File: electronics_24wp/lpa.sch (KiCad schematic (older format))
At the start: 28 parts, among them IC1 ATMEGA328-A, P1 CONN_2, P2 CONN_3X2, U1 SD_CARD, U2 LD1117S33, X1 CRYSTAL_SMD

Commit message: Changed orientation of error LED.
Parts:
- ERR1: symbol LED -> LED-INV
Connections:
- net GND: now also ERR1.2 (K); no longer ERR1.1 (K)
- net at R_ERR1.2: now also ERR1.1 (A); no longer ERR1.2 (A)
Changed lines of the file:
@@
 $EndComp
 $Comp
-L LED ERR1
+L LED-INV ERR1
 U 1 1 5356E77E
 P 4750 6550
@@
 F 3 "~" H 4750 6550 60  0000 C CNN
 	1    4750 6550
-	-1   0    0    -1
+	1    0    0    1
 $EndComp
 $Comp

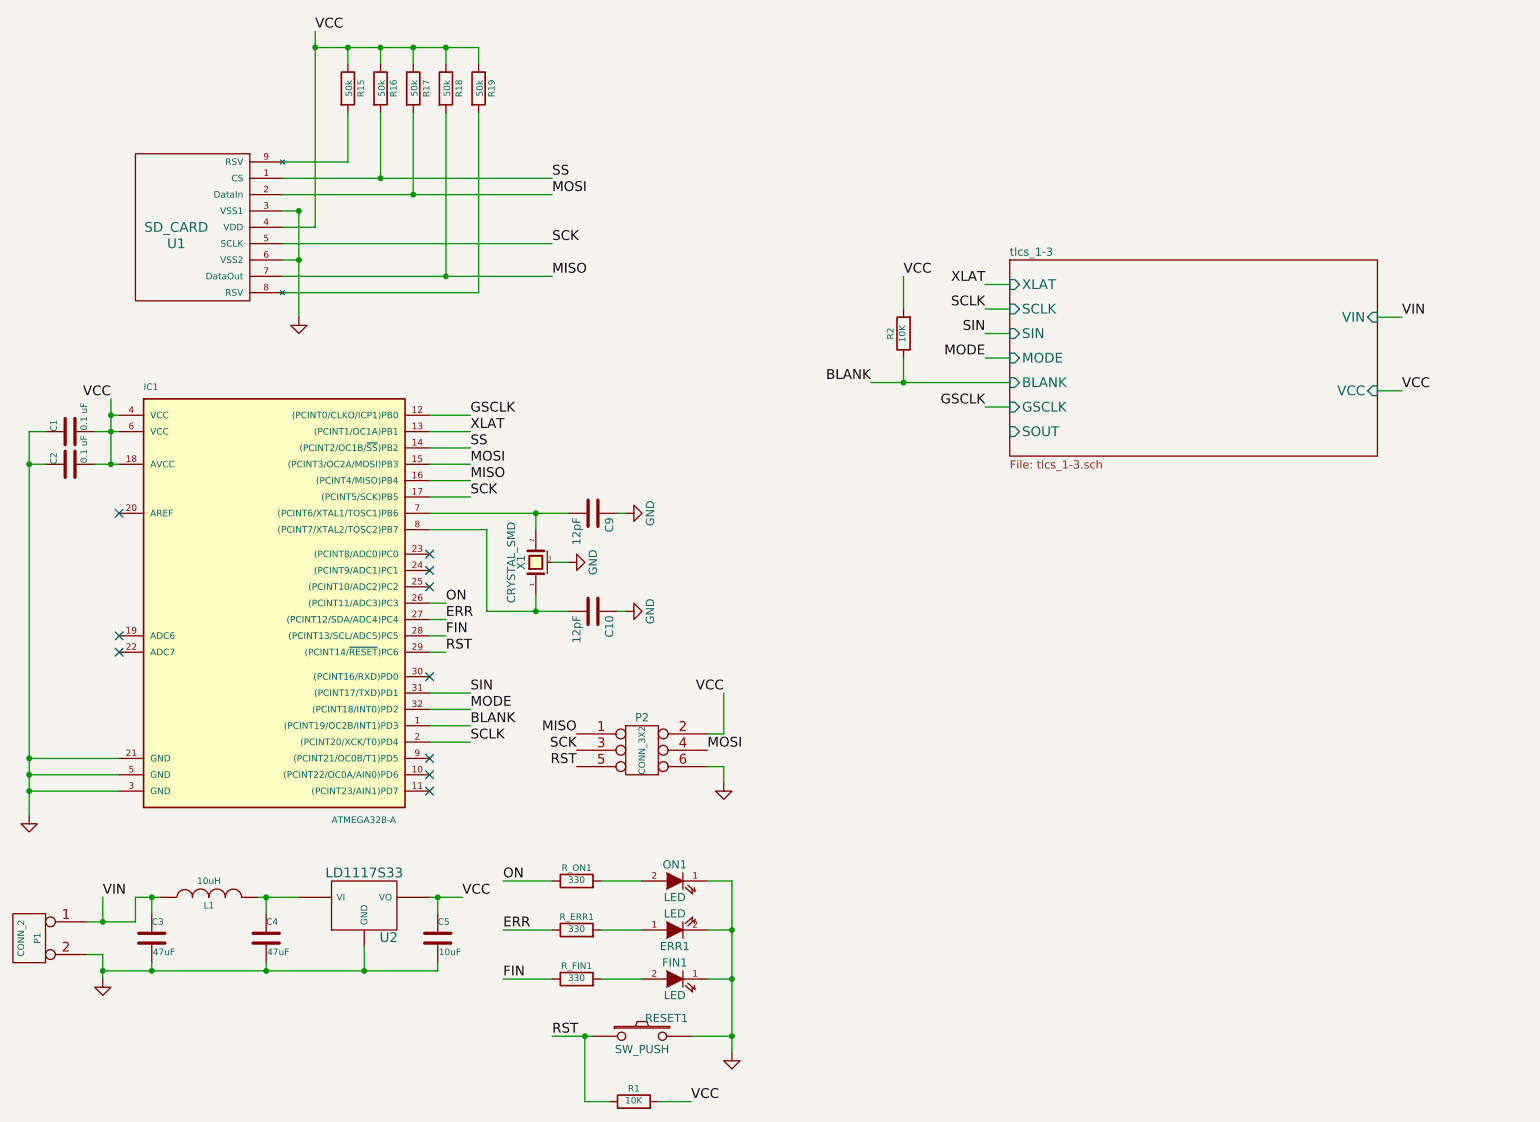
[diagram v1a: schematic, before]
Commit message: Removed pullup resistors from SD card socket.
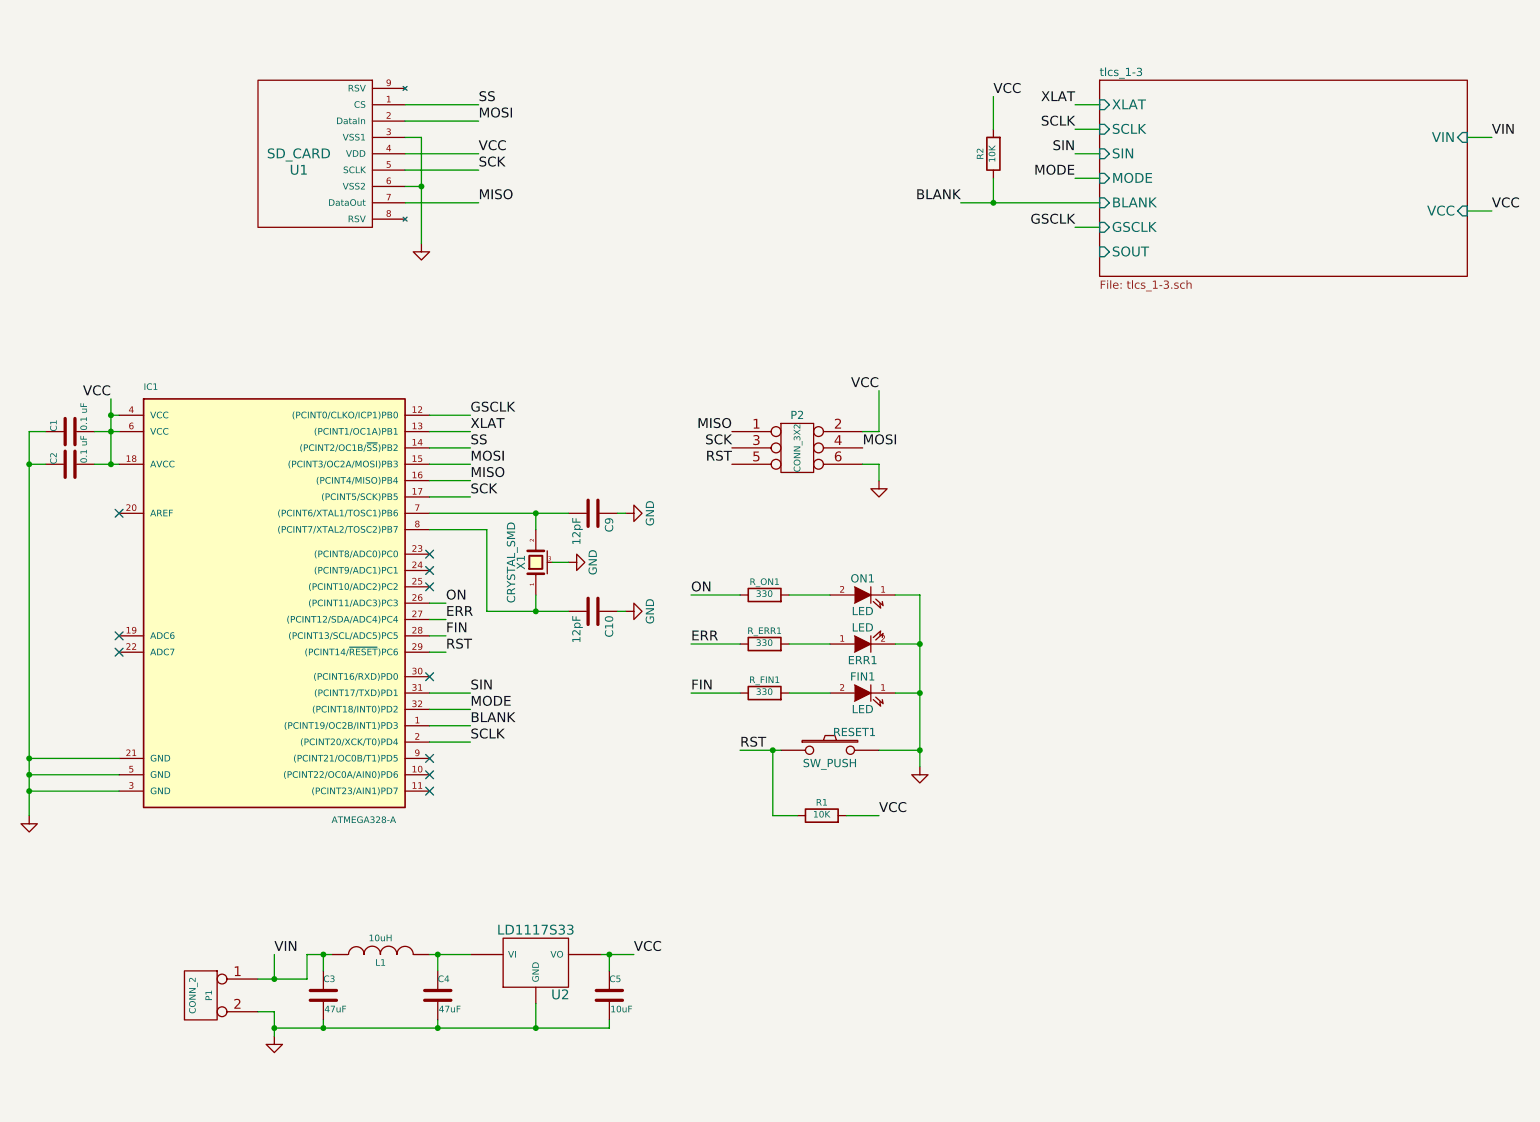
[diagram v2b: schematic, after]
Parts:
- removed R15, R16, R17, R18, R19: 50k, LPA_parts:SM0805, symbol R
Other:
- moved on the sheet: C3, C4, C5, ERR1, FIN1, L1, ON1, P1, P2, R1, R2, RESET1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

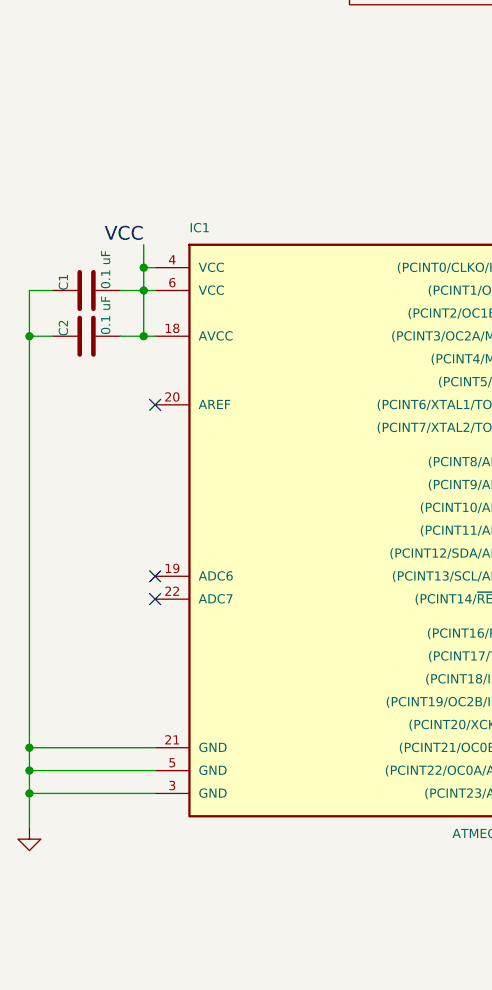
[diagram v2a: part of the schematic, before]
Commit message: Added one more decoupling resistor to uC.
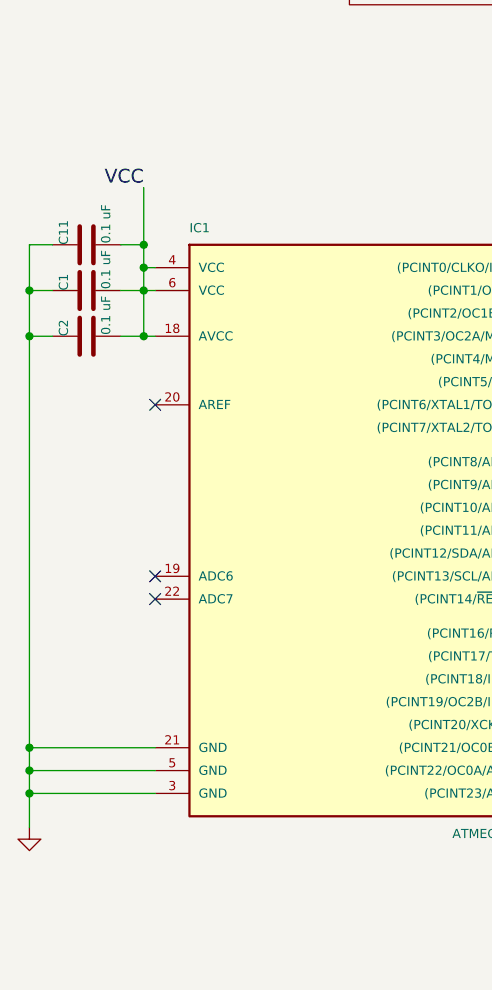
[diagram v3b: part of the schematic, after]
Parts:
- added C11: 0.1 uF, LPA_parts:SM0805, symbol C
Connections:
- net GND: now also C11.1
- net VCC: now also C11.2
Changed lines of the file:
@@
 Text Label 3500 3500 0    60   ~ 0
 XLAT
-Text Label 1300 3300 2    60   ~ 0
+Text Label 1300 3050 2    60   ~ 0
 VCC
 NoConn ~ 1350 4000
@@
 Wire Wire Line
 	3250 5100 3500 5100
-Wire Wire Line
-	800  3500 900  3500
 Connection ~ 800  3700
-Wire Wire Line
-	800  3700 900  3700
 Wire Wire Line
 	3600 4600 4100 4600
@@
 	1200 3700 1350 3700
 Wire Wire Line
-	1300 3300 1300 3700
+	1300 3050 1300 3700
 Wire Wire Line
 	1350 3400 1300 3400
@@
 	1200 3500 1350 3500
 Wire Wire Line
-	800  3500 800  5850
+	800  3300 800  5850
 Wire Wire Line
 	800  5500 1350 5500
@@
 Wire Wire Line
 	5450 4500 5700 4500
+Wire Wire Line
+	800  3500 900  3500
+Wire Wire Line
+	800  3700 900  3700
+$Comp
+L C C11
+U 1 1 569F3F37
+P 1050 3300
+F 0 "C11" H 1050 3400 40  0000 L CNN
+F 1 "0.1 uF" H 1056 3215 40  0000 L CNN
+F 2 "LPA_parts:SM0805" H 1088 3150 30  0001 C CNN
+F 3 "~" H 1050 3300 60  0000 C CNN
+	1    1050 3300
+	0    -1   -1   0
+$EndComp
+Wire Wire Line
+	800  3300 900  3300
+Connection ~ 800  3500
+Wire Wire Line
+	1200 3300 1300 3300
+Connection ~ 1300 3300
 $EndSCHEMATC

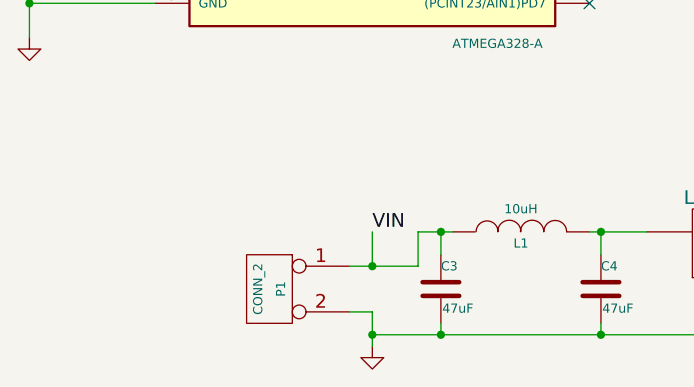
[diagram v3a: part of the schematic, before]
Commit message: Replaced power connector by barrel jack.
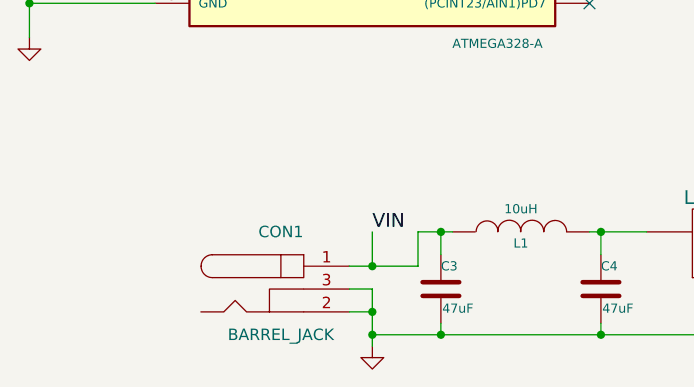
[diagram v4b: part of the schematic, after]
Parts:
- removed P1: CONN_2, LPA_parts:CONNECTOR_2X1_3960um, symbol CONN_2
- added CON1: BARREL_JACK, Connect:BARREL_JACK, symbol BARREL_JACK
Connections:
- net GND: now also CON1.2, CON1.3
- net VIN: now also CON1.1
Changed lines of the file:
@@
 VCC
-$Comp
-L CONN_2 P1
-U 1 1 5213FDDC
-P 1850 6950
-F 0 "P1" V 1800 6950 40  0000 C CNN
-F 1 "CONN_2" V 1900 6950 40  0000 C CNN
-F 2 "LPA_parts:CONNECTOR_2X1_3960um" H 1850 6950 60  0001 C CNN
-F 3 "" H 1850 6950 60  0000 C CNN
-	1    1850 6950
-	-1   0    0    -1
-$EndComp
 $Comp
 L CONN_3X2 P2
@@
 	2500 6850 2500 6700
 Wire Wire Line
-	2300 7050 2300 7200
+	2300 6950 2300 7200
 Wire Wire Line
 	2200 7050 2300 7050
@@
 	1200 3300 1300 3300
 Connection ~ 1300 3300
+$Comp
+L BARREL_JACK CON1
+U 1 1 56A00A09
+P 1900 6950
+F 0 "CON1" H 1900 7200 50  0000 C CNN
+F 1 "BARREL_JACK" H 1900 6750 50  0000 C CNN
+F 2 "Connect:BARREL_JACK" H 1900 6950 50  0001 C CNN
+F 3 "" H 1900 6950 50  0000 C CNN
+	1    1900 6950
+	1    0    0    -1
+$EndComp
+Wire Wire Line
+	2200 6950 2300 6950
+Connection ~ 2300 7050
 $EndSCHEMATC

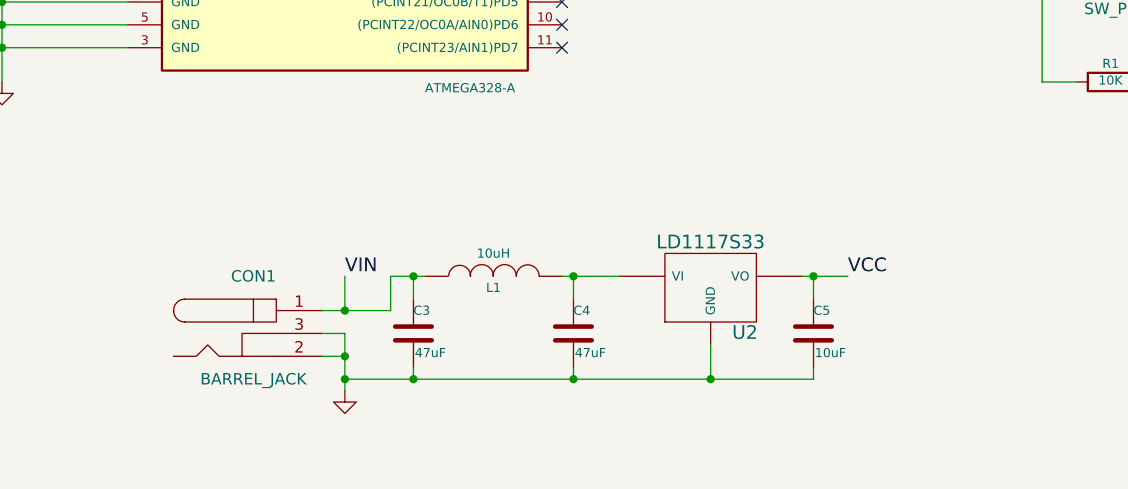
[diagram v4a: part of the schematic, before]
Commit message: Changed power supply circuit.
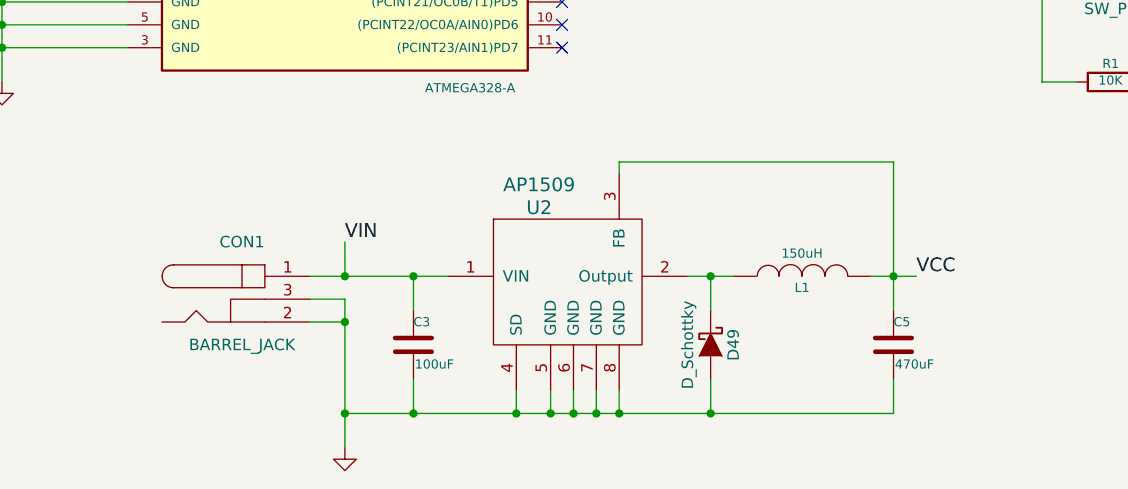
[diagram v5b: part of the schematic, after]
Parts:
- removed C4: 47uF, c_elec_6.3x5.3, symbol C
- removed U2: LD1117S33, SOT223, symbol LD1117S50
- added D49: D_Schottky, Diodes_SMD:SOD-123, symbol D_Schottky
- added U2: AP1509, Housings_SOIC:SOIC-8_3.9x4.9mm_Pitch1.27mm, symbol AP1509
- C3: value 47uF -> 100uF; footprint c_elec_6.3x5.3 -> Capacitors_SMD:c_elec_6.3x7.7
- C5: value 10uF -> 470uF; footprint LPA_parts:SM0805 -> Capacitors_SMD:c_elec_8x10
- L1: value 10uH -> 150uH; footprint SM1210 -> LPA_parts:Inductor
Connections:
- net GND: now also D49.2 (A), U2.4 (SD), U2.5 (GND), U2.6 (GND), U2.7 (GND), U2.8 (GND)
- net VCC: now also L1.2, U2.3 (FB)
- net VIN: now also U2.1 (VIN); no longer L1.1
- new net: D49.1 (K), L1.1, U2.2 (Output)
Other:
- moved on the sheet: C3, C5, CON1, L1
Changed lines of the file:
@@
 L C C5
 U 1 1 535704C8
-P 4350 6950
-F 0 "C5" H 4350 7050 40  0000 L CNN
-F 1 "10uF" H 4356 6865 40  0000 L CNN
-F 2 "LPA_parts:SM0805" H 4388 6800 30  0001 C CNN
-F 3 "~" H 4350 6950 60  0000 C CNN
-	1    4350 6950
+P 4700 7000
+F 0 "C5" H 4700 7100 40  0000 L CNN
+F 1 "470uF" H 4706 6915 40  0000 L CNN
+F 2 "Capacitors_SMD:c_elec_8x10" H 4738 6850 30  0001 C CNN
+F 3 "~" H 4700 7000 60  0000 C CNN
+	1    4700 7000
 	1    0    0    -1
 $EndComp
@@
 L C C3
 U 1 1 535704B9
-P 2600 6950
-F 0 "C3" H 2600 7050 40  0000 L CNN
-F 1 "47uF" H 2606 6865 40  0000 L CNN
-F 2 "c_elec_6.3x5.3" H 2638 6800 30  0001 C CNN
-F 3 "~" H 2600 6950 60  0000 C CNN
-	1    2600 6950
-	1    0    0    -1
-$EndComp
-$Comp
-L LD1117S50 U2
-U 1 1 5357046B
-P 3900 6750
-F 0 "U2" H 4050 6554 60  0000 C CNN
-F 1 "LD1117S33" H 3900 6950 60  0000 C CNN
-F 2 "SOT223" H 3900 6750 60  0001 C CNN
-F 3 "~" H 3900 6750 60  0000 C CNN
-	1    3900 6750
-	1    0    0    -1
-$EndComp
-Text Label 2300 6700 0    60   ~ 0
+P 2600 7000
+F 0 "C3" H 2600 7100 40  0000 L CNN
+F 1 "100uF" H 2606 6915 40  0000 L CNN
+F 2 "Capacitors_SMD:c_elec_6.3x7.7" H 2638 6850 30  0001 C CNN
+F 3 "~" H 2600 7000 60  0000 C CNN
+	1    2600 7000
+	1    0    0    -1
+$EndComp
+Text Label 2300 6550 0    60   ~ 0
 VIN
 Text Label 4850 5100 0    60   ~ 0
@@
 L GND #PWR05
 U 1 1 5214D369
-P 2300 7200
-F 0 "#PWR05" H 2300 7200 30  0001 C CNN
-F 1 "GND" H 2300 7130 30  0001 C CNN
-F 2 "" H 2300 7200 60  0000 C CNN
-F 3 "" H 2300 7200 60  0000 C CNN
-	1    2300 7200
-	1    0    0    -1
-$EndComp
-Text Label 4500 6700 0    60   ~ 0
+P 2300 7450
+F 0 "#PWR05" H 2300 7450 30  0001 C CNN
+F 1 "GND" H 2300 7380 30  0001 C CNN
+F 2 "" H 2300 7450 60  0000 C CNN
+F 3 "" H 2300 7450 60  0000 C CNN
+	1    2300 7450
+	1    0    0    -1
+$EndComp
+Text Label 4800 6700 0    60   ~ 0
 VCC
 $Comp
@@
 L INDUCTOR L1
 U 1 1 53AA01D0
-P 2950 6700
-F 0 "L1" V 2900 6700 40  0000 C CNN
-F 1 "10uH" V 3050 6700 40  0000 C CNN
-F 2 "SM1210" H 2950 6700 60  0001 C CNN
-F 3 "~" H 2950 6700 60  0000 C CNN
-	1    2950 6700
-	0    -1   -1   0
-$EndComp
-$Comp
-L C C4
-U 1 1 53AA0322
-P 3300 6950
-F 0 "C4" H 3300 7050 40  0000 L CNN
-F 1 "47uF" H 3306 6865 40  0000 L CNN
-F 2 "c_elec_6.3x5.3" H 3338 6800 30  0001 C CNN
-F 3 "~" H 3300 6950 60  0000 C CNN
-	1    3300 6950
-	1    0    0    -1
+P 4300 6700
+F 0 "L1" V 4250 6700 40  0000 C CNN
+F 1 "150uH" V 4400 6700 40  0000 C CNN
+F 2 "LPA_parts:Inductor" H 4300 6700 60  0001 C CNN
+F 3 "~" H 4300 6700 60  0000 C CNN
+	1    4300 6700
+	0    -1   -1   0
 $EndComp
 Wire Wire Line
@@
 	3100 1500 3550 1500
 Wire Wire Line
-	4350 6700 4350 6800
-Connection ~ 4350 6700
-Wire Wire Line
-	4300 6700 4500 6700
-Connection ~ 3900 7150
-Wire Wire Line
-	3900 7150 3900 7000
-Connection ~ 2300 7150
-Connection ~ 2600 6700
-Wire Wire Line
-	2600 6700 2600 6800
-Connection ~ 2300 6850
-Wire Wire Line
-	2500 6700 2650 6700
-Wire Wire Line
-	2500 6850 2500 6700
-Wire Wire Line
-	2300 6950 2300 7200
-Wire Wire Line
-	2200 7050 2300 7050
-Wire Wire Line
-	2300 6850 2300 6700
-Wire Wire Line
-	2200 6850 2500 6850
+	4700 6200 4700 6850
+Connection ~ 4700 6700
+Wire Wire Line
+	4600 6700 4800 6700
+Connection ~ 2300 7300
+Wire Wire Line
+	2600 6700 2600 6850
+Connection ~ 2300 6700
+Wire Wire Line
+	2150 6700 2750 6700
+Wire Wire Line
+	2300 6800 2300 7450
+Wire Wire Line
+	2150 6900 2300 6900
+Wire Wire Line
+	2300 6700 2300 6550
 Wire Wire Line
 	5800 5850 6000 5850
@@
 Connection ~ 6700 2100
 Wire Wire Line
-	3250 6700 3500 6700
-Wire Wire Line
-	3300 6700 3300 6800
-Connection ~ 3300 6700
-Wire Wire Line
-	2300 7150 4350 7150
-Connection ~ 2600 7150
-Connection ~ 3300 7150
+	2300 7300 4700 7300
+Connection ~ 2600 7300
 Wire Wire Line
 	3200 1700 3200 2350
@@
 	4000 4300 4100 4300
 Wire Wire Line
-	2600 7100 2600 7150
-Wire Wire Line
-	3300 7100 3300 7150
-Wire Wire Line
-	4350 7150 4350 7100
+	2600 7300 2600 7150
+Wire Wire Line
+	4700 7300 4700 7150
 Wire Wire Line
 	6100 4500 6250 4500
@@
 L BARREL_JACK CON1
 U 1 1 56A00A09
-P 1900 6950
-F 0 "CON1" H 1900 7200 50  0000 C CNN
-F 1 "BARREL_JACK" H 1900 6750 50  0000 C CNN
-F 2 "Connect:BARREL_JACK" H 1900 6950 50  0001 C CNN
-F 3 "" H 1900 6950 50  0000 C CNN
-	1    1900 6950
-	1    0    0    -1
-$EndComp
-Wire Wire Line
-	2200 6950 2300 6950
-Connection ~ 2300 7050
+P 1850 6800
+F 0 "CON1" H 1850 7050 50  0000 C CNN
+F 1 "BARREL_JACK" H 1850 6600 50  0000 C CNN
+F 2 "Connect:BARREL_JACK" H 1850 6800 50  0001 C CNN
+F 3 "" H 1850 6800 50  0000 C CNN
+	1    1850 6800
+	1    0    0    -1
+$EndComp
+Wire Wire Line
+	2150 6800 2300 6800
+Connection ~ 2300 6900
+$Comp
+L D_Schottky D49
+U 1 1 56A0443A
+P 3900 7000
+F 0 "D49" H 3900 7100 50  0000 C CNN
+F 1 "D_Schottky" H 3900 6900 50  0000 C CNN
+F 2 "Diodes_SMD:SOD-123" H 3900 7000 50  0001 C CNN
+F 3 "" H 3900 7000 50  0000 C CNN
+	1    3900 7000
+	0    1    1    0
+$EndComp
+Wire Wire Line
+	3900 7300 3900 7150
+Connection ~ 3900 7300
+Wire Wire Line
+	3800 6700 4000 6700
+Wire Wire Line
+	3900 6700 3900 6850
+$Comp
+L AP1509 U2
+U 1 1 56A062A4
+P 3250 6700
+F 0 "U2" H 3150 7000 60  0000 C CNN
+F 1 "AP1509" H 3150 7100 60  0000 C CNN
+F 2 "Housings_SOIC:SOIC-8_3.9x4.9mm_Pitch1.27mm" H 3250 6700 60  0001 C CNN
+F 3 "" H 3250 6700 60  0000 C CNN
+	1    3250 6700
+	1    0    0    -1
+$EndComp
+Wire Wire Line
+	3500 6250 3500 6200
+Wire Wire Line
+	3500 6200 4700 6200
+Connection ~ 3900 6700
+Connection ~ 2600 6700
+Wire Wire Line
+	3050 7200 3050 7300
+Connection ~ 3050 7300
+Wire Wire Line
+	3200 7200 3200 7300
+Connection ~ 3200 7300
+Wire Wire Line
+	3300 7200 3300 7300
+Connection ~ 3300 7300
+Wire Wire Line
+	3400 7200 3400 7300
+Connection ~ 3400 7300
+Wire Wire Line
+	3500 7200 3500 7300
+Connection ~ 3500 7300
 $EndSCHEMATC

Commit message: Changed barrel jack pads to circular.
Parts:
- CON1: footprint Connect:BARREL_JACK -> LPA_parts:BARREL_JACK_CIRCULAR_PADS
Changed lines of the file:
@@
 F 0 "CON1" H 1850 7050 50  0000 C CNN
 F 1 "BARREL_JACK" H 1850 6600 50  0000 C CNN
-F 2 "Connect:BARREL_JACK" H 1850 6800 50  0001 C CNN
+F 2 "LPA_parts:BARREL_JACK_CIRCULAR_PADS" H 1850 6800 50  0001 C CNN
 F 3 "" H 1850 6800 50  0000 C CNN
 	1    1850 6800
